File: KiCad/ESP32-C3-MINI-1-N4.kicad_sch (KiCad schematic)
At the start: 19 parts, among them U2 ESP32-C3-MINI-1-N4

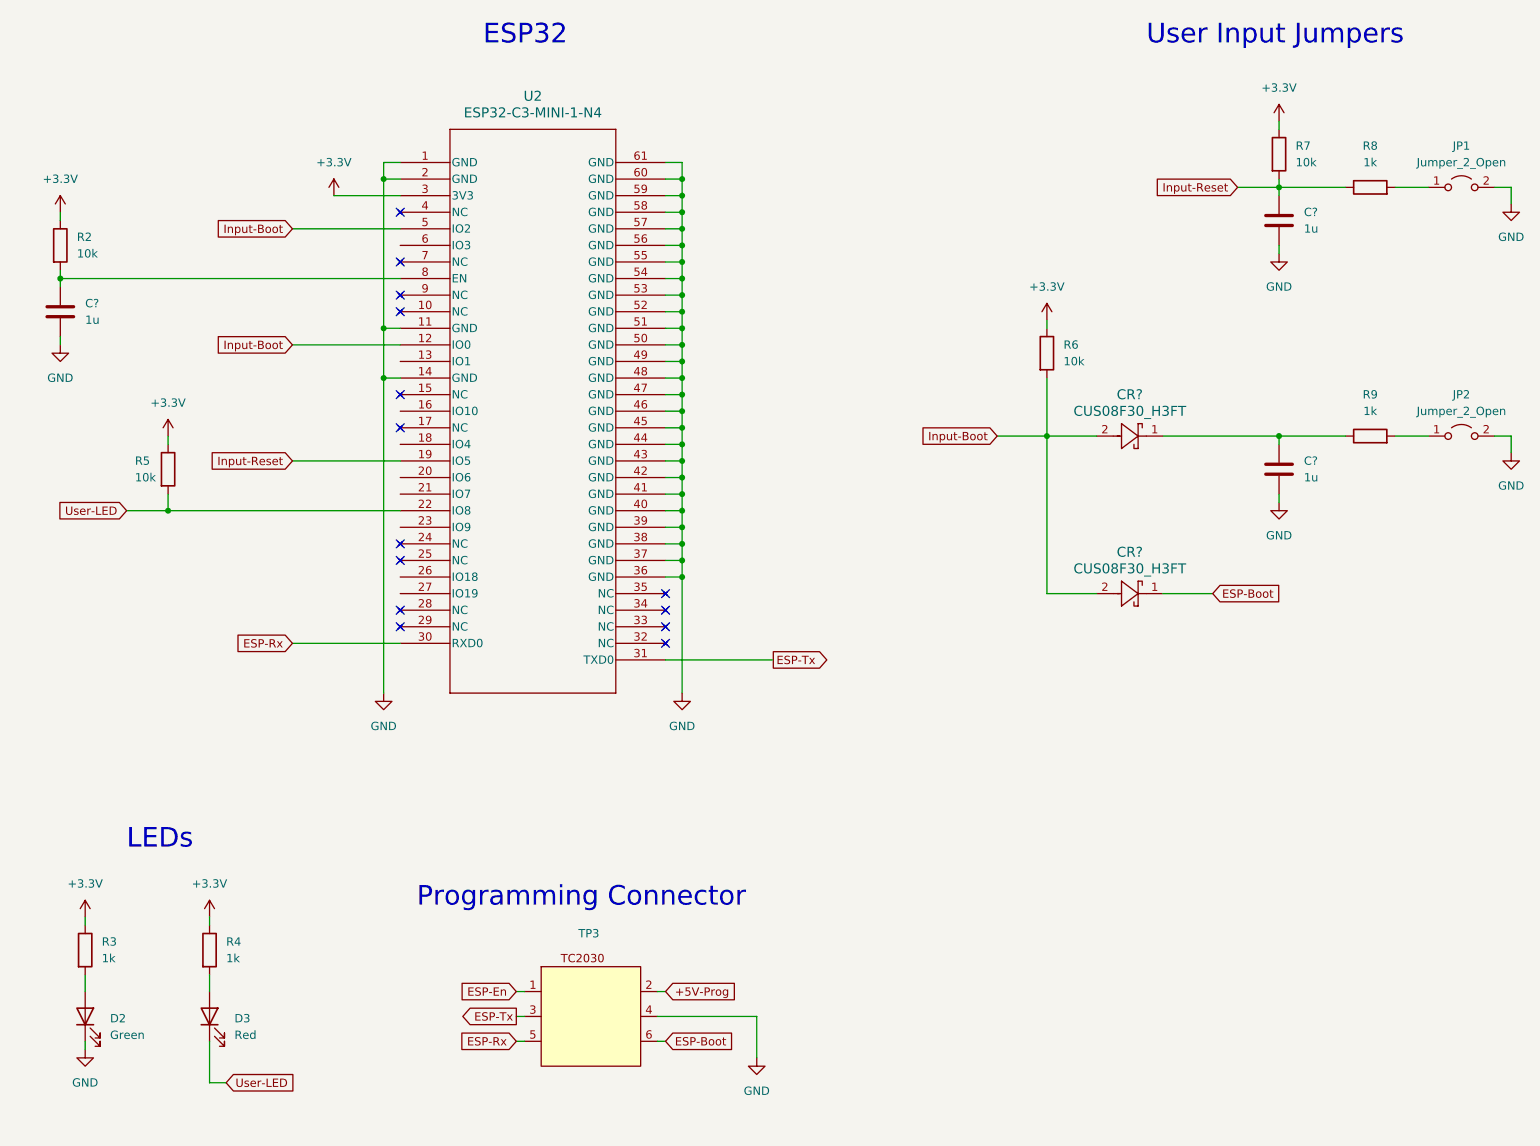
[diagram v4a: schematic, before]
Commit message: Use load switch, fix TC2030 pins, fix strapping pins
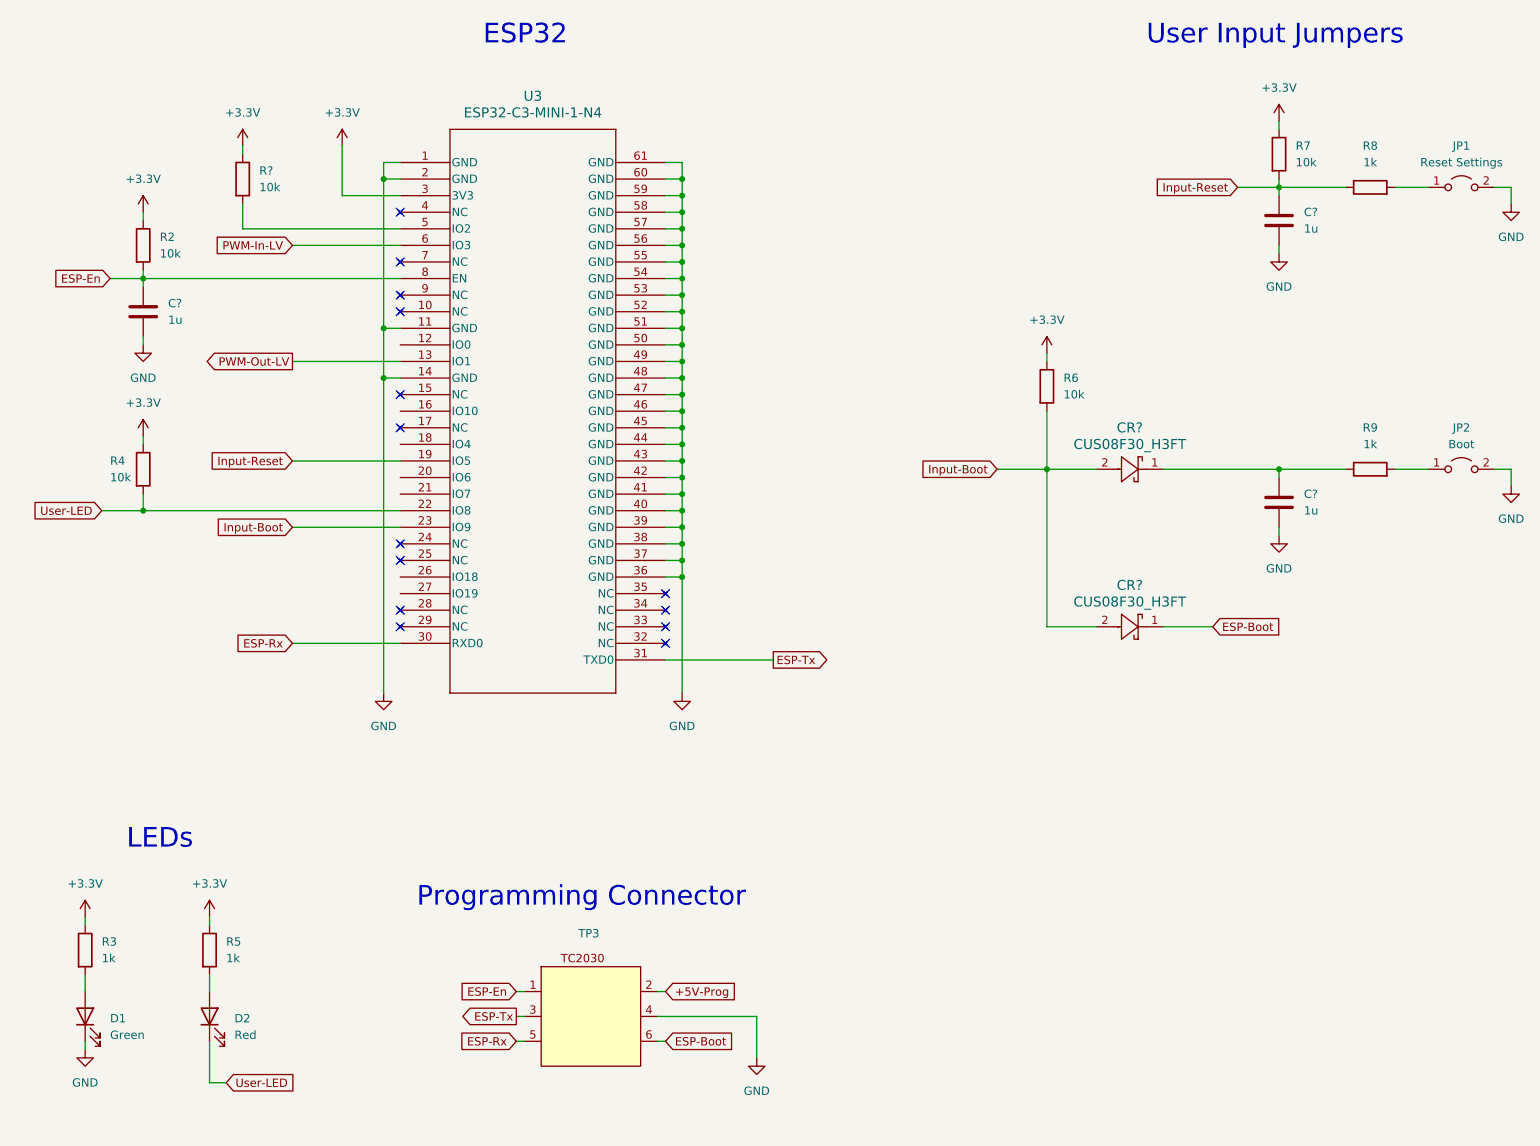
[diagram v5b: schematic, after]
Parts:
- added R?: 10k, Resistor_SMD:R_0402_1005Metric_Pad0.72x0.64mm_HandSolder, symbol Device:R
- JP1: value Jumper_2_Open -> Reset Settings
- JP2: value Jumper_2_Open -> Boot
- renumbered D2 to D1, D3 to D2, R5 to R4, R4 to R5, U2 to U3
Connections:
- net +3.3V: now also R?.1
- net ESP-En: now also C?.1, R2.2, U3.8 (EN)
- net Input-Boot: now also U3.23 (IO9); no longer U3.12 (IO0), U3.5 (IO2)
- net PWM-Out-LV: now reaches U3.13 (IO1)
- net PWM-In-LV: now reaches U3.6 (IO3)
- new net: R?.2, U3.5 (IO2)
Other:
- company: (none) -> Tamás Nagy
- title: (none) -> Hydrofoil Control
- moved on the sheet: C?, CR?, JP2, R2, R4, R6, R9
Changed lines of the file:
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@@
 (kicad_sch (version 20230121) (generator eeschema)
   (paper "A4")
+  (title_block
+    (title "Hydrofoil Control")
+    (date "2023-09-04")
+    (rev "v1.0")
+    (company "Tamás Nagy")
+  )

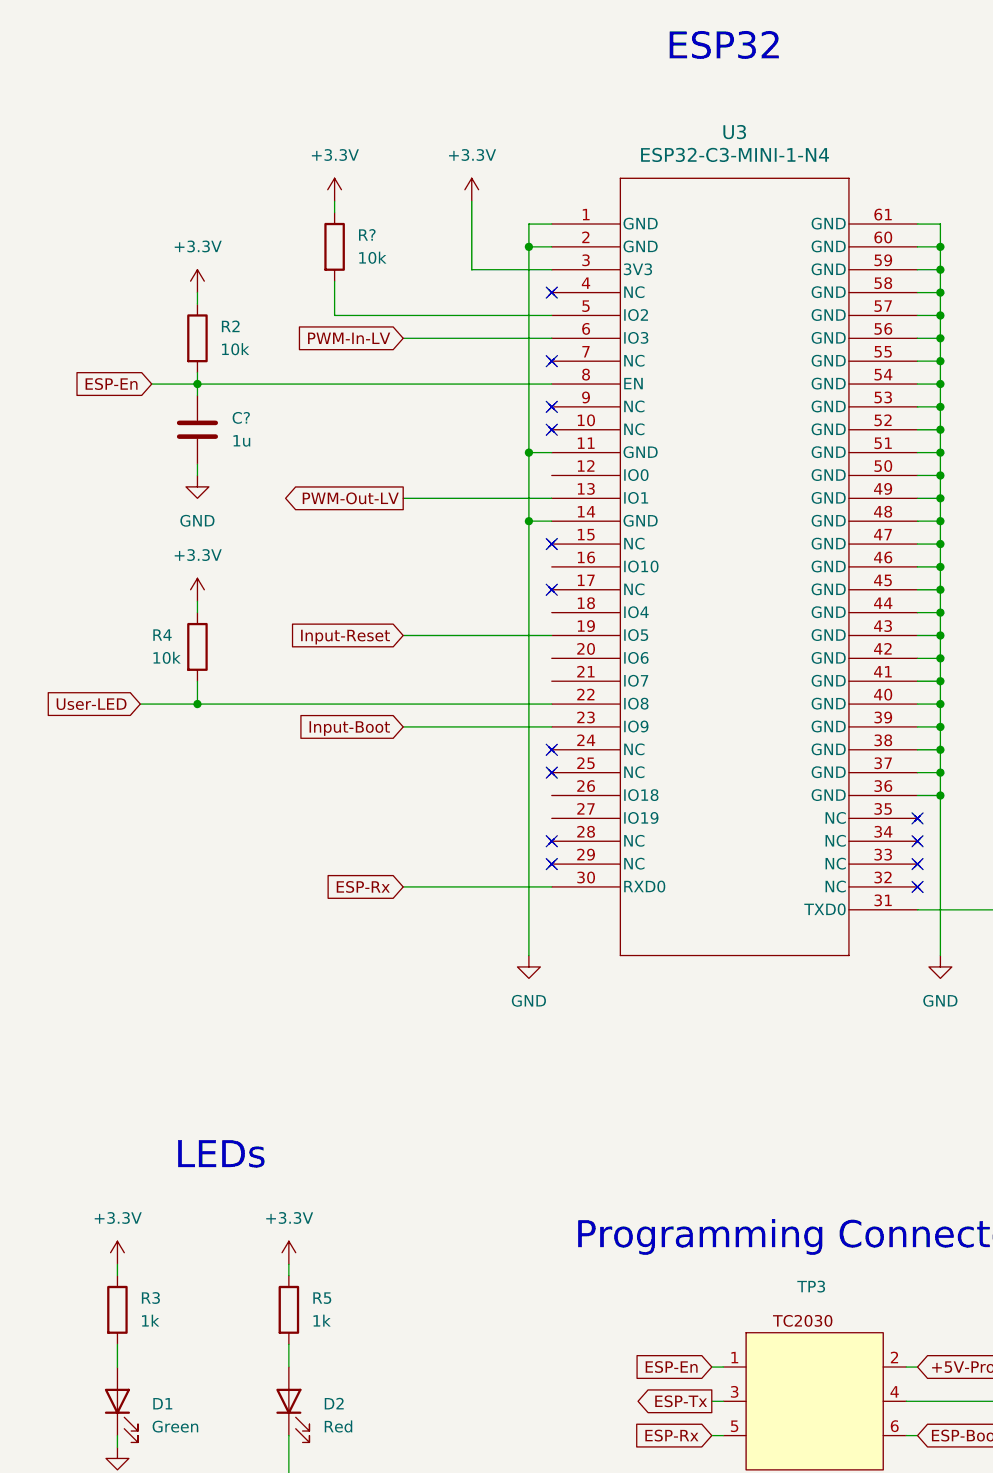
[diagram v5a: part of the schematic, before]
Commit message: Organize parts on the PCB
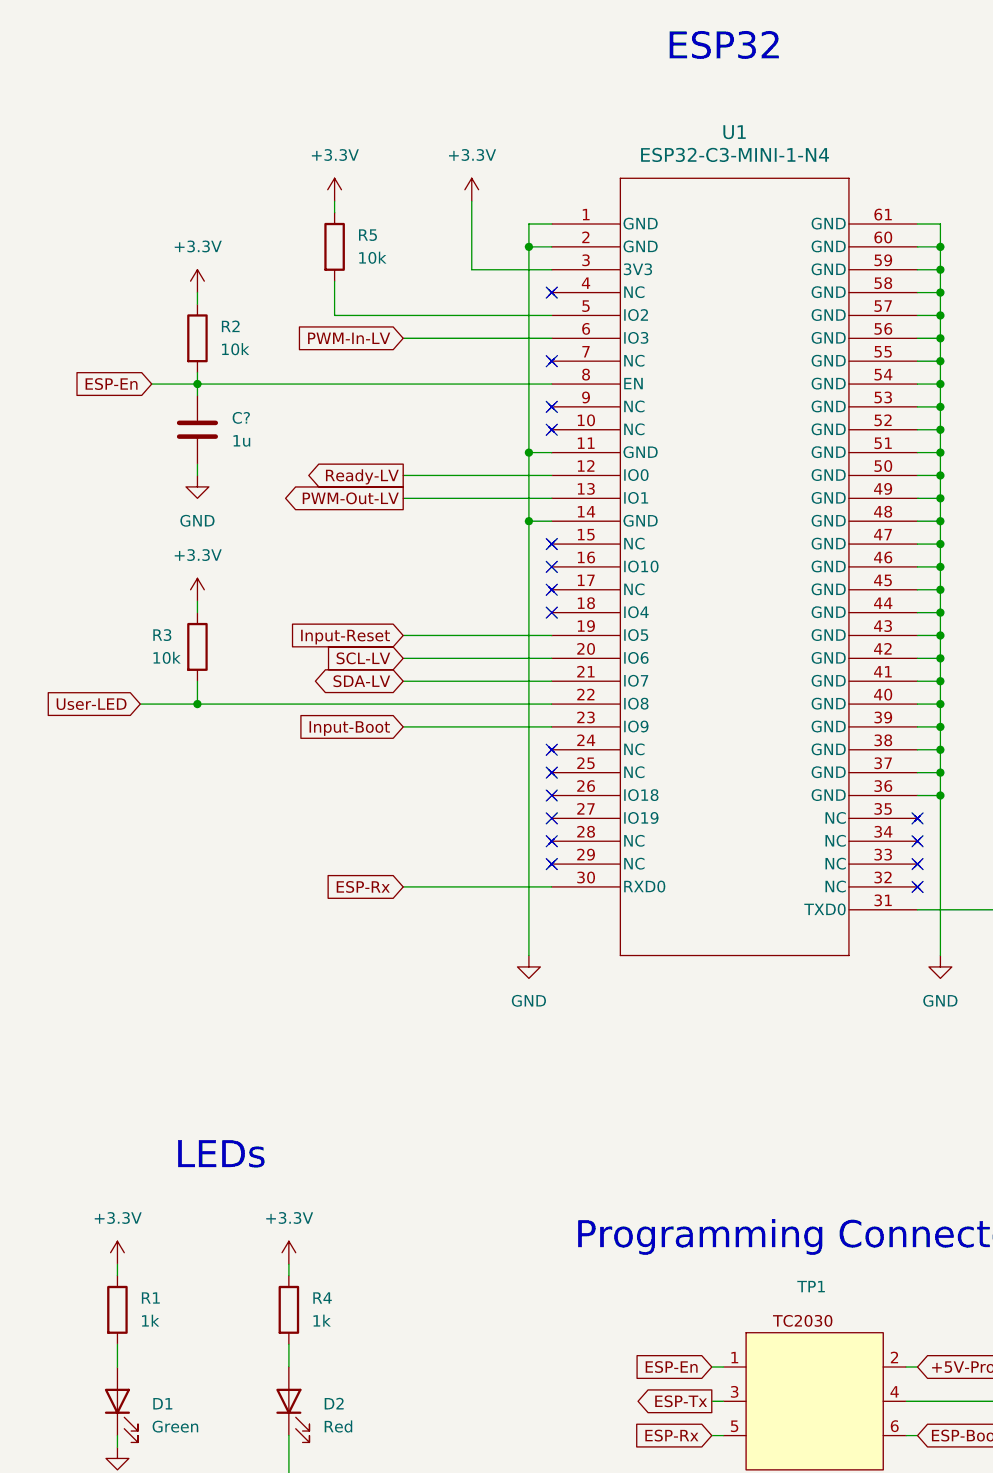
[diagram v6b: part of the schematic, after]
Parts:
- gave numbers to parts that had none: 1
- renumbered R3 to R1, R4 to R3, R5 to R4, TP3 to TP1, U3 to U1
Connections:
- net Ready-LV: now reaches U1.12 (IO0)
- net SCL-LV: now reaches U1.20 (IO6)
- net SDA-LV: now reaches U1.21 (IO7)
- no-connect marks 14 -> 18
